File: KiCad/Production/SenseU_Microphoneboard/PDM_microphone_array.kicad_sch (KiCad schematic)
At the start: 12 parts

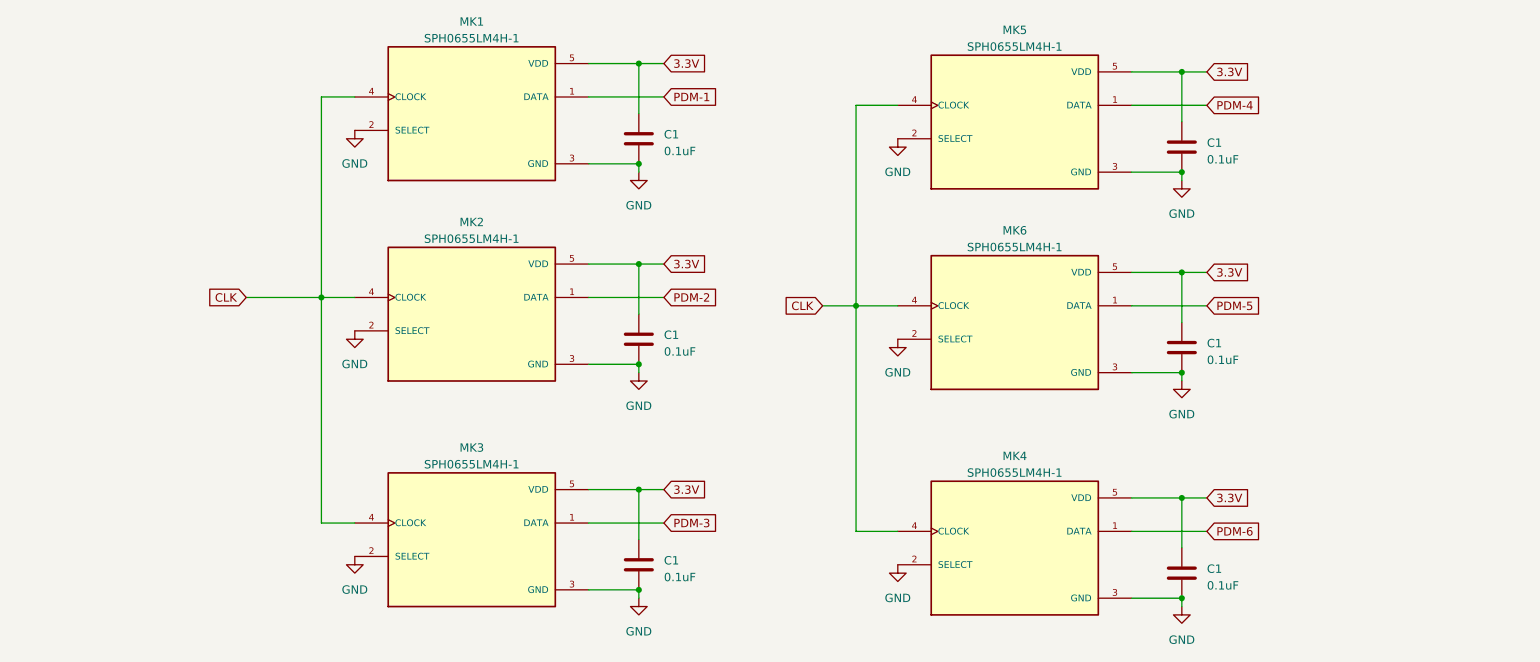
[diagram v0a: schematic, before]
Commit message: PCB V1 finished (9 MEMS), DRC violation rules pending
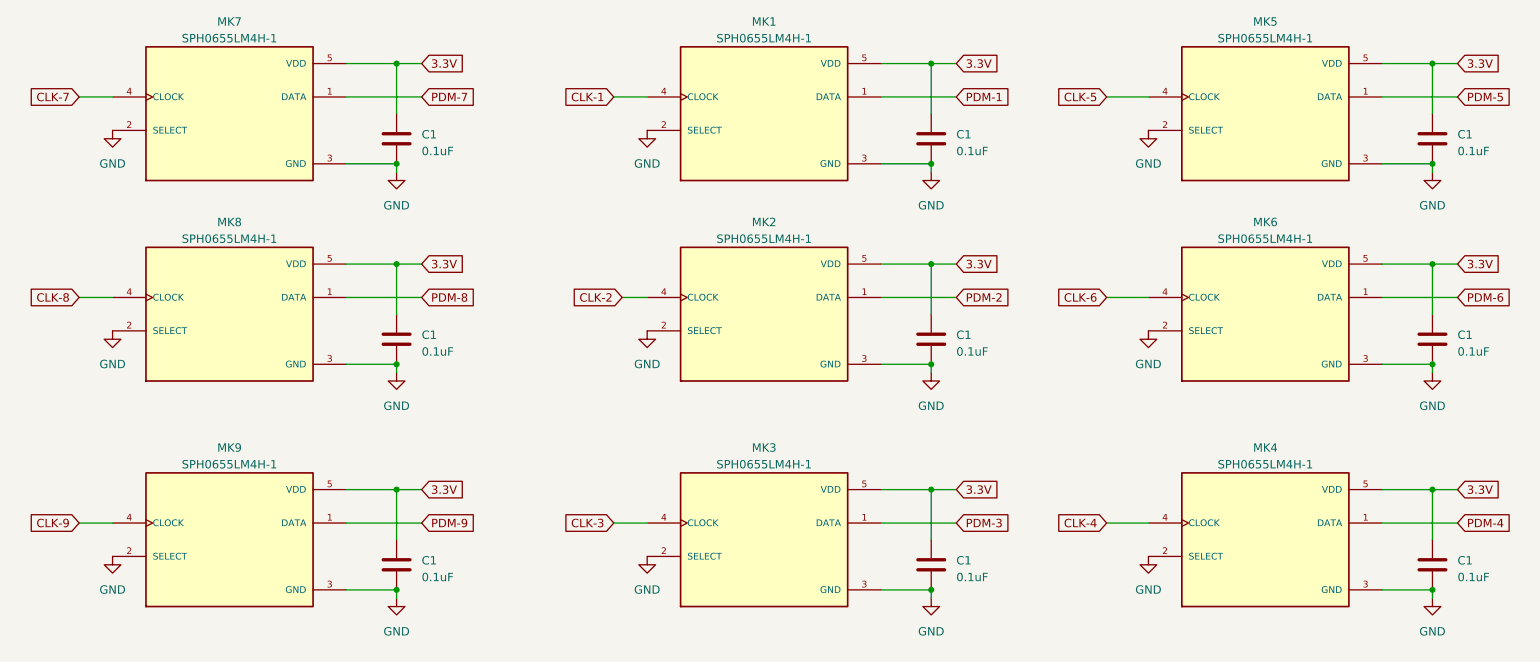
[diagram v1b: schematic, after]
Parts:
- added C1 (x3): 0.1uF, Capacitor_SMD:C_0603_1608Metric_Pad1.08x0.95mm_HandSolder, symbol Device:C
- added MK7, MK8, MK9: SPH0655LM4H-1, SenseU_Microphoneboard:MIC_SPH0655LM4H-1, symbol SensU_Microphone_parts:SPH0655LM4H-1
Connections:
- net 3.3V: now also C1.1, C1.1, C1.1, MK7.5 (VDD), MK8.5 (VDD), MK9.5 (VDD)
- net GND: now also C1.2, C1.2, C1.2, MK7.2 (SELECT), MK7.3 (GND), MK8.2 (SELECT), MK8.3 (GND), MK9.2 (SELECT), MK9.3 (GND)
- net PDM-4: now also MK4.1 (DATA); no longer MK5.1 (DATA)
- net PDM-5: now also MK5.1 (DATA); no longer MK6.1 (DATA)
- net PDM-6: now also MK6.1 (DATA); no longer MK4.1 (DATA)
- removed net CLK: MK1.4 (CLOCK), MK2.4 (CLOCK), MK3.4 (CLOCK), MK4.4 (CLOCK), MK5.4 (CLOCK), MK6.4 (CLOCK)
- new net CLK-1: MK1.4 (CLOCK)
- new net CLK-2: MK2.4 (CLOCK)
- new net CLK-3: MK3.4 (CLOCK)
- new net CLK-4: MK4.4 (CLOCK)
- new net CLK-5: MK5.4 (CLOCK)
- new net CLK-6: MK6.4 (CLOCK)
- new net CLK-7: MK7.4 (CLOCK)
- new net CLK-8: MK8.4 (CLOCK)
- new net CLK-9: MK9.4 (CLOCK)
- new net PDM-7: MK7.1 (DATA)
- new net PDM-8: MK8.1 (DATA)
- new net PDM-9: MK9.1 (DATA)
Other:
- moved on the sheet: C1, MK1, MK2, MK3, MK4, MK5, MK6
